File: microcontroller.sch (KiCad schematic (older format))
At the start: 21 parts, among them J4 Conn_01x02, J6 I2C, J7 Conn_01x02, J8 I2C, SW1 SW_Push, U3 ESP32-DEVKIT

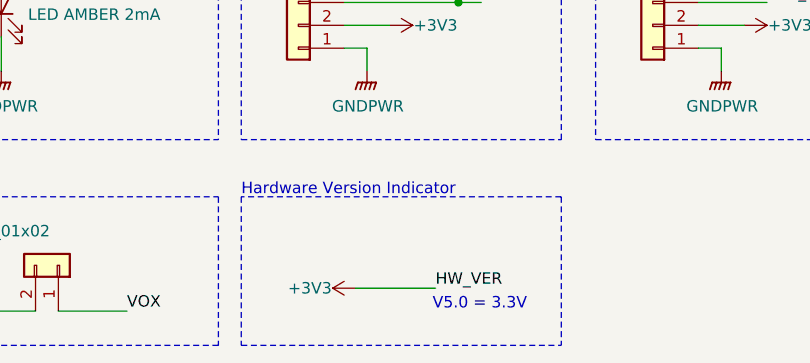
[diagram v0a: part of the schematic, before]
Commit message: Added Pullup to HW indicator [#25]
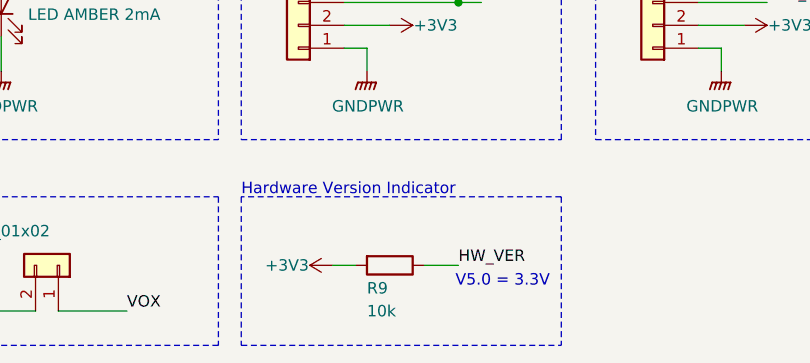
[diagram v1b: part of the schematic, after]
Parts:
- added R9: 10k, Resistor_SMD:R_0805_2012Metric_Pad1.15x1.40mm_HandSolder, symbol Device:R
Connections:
- net +3V3: now also R9.2; no longer U3.5 (IO34)
- new net HW_VER: R9.1, U3.5 (IO34)
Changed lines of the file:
@@
 Text Notes 2250 5700 0    50   ~ 0
 Hardware Version Indicator
-Text Label 3100 6100 0    50   ~ 0
+Text Label 3200 6000 0    50   ~ 0
 HW_VER
 Wire Notes Line
 	2250 6350 3650 6350
-Wire Wire Line
-	2750 6100 3100 6100
-Text Notes 3500 6200 2    50   ~ 0
+Text Notes 3600 6100 2    50   ~ 0
 V5.0 = 3.3V
 Wire Notes Line
 	3650 5700 3650 6350
-Wire Notes Line
-	2250 5700 2250 6350
-Wire Notes Line
-	2150 5700 2150 6350
 Wire Notes Line
 	700  5700 700  6350
@@
 L power:+3V3 #PWR?
 U 1 1 5E2D79C9
-P 2750 6100
+P 2650 6000
 AR Path="/5E2D79C9" Ref="#PWR?"  Part="1"
 AR Path="/5C10B93A/5E2D79C9" Ref="#PWR045"  Part="1"
-F 0 "#PWR045" H 2750 5950 50  0001 C CNN
-F 1 "+3V3" V 2750 6300 50  0000 C CNN
-F 2 "" H 2750 6100 50  0001 C CNN
-F 3 "" H 2750 6100 50  0001 C CNN
-	1    2750 6100
+F 0 "#PWR045" H 2650 5850 50  0001 C CNN
+F 1 "+3V3" V 2650 6200 50  0000 C CNN
+F 2 "" H 2650 6000 50  0001 C CNN
+F 3 "" H 2650 6000 50  0001 C CNN
+	1    2650 6000
 	0    -1   -1   0
 $EndComp
@@
 	1    0    0    -1
 $EndComp
+Wire Notes Line
+	2150 5700 2150 6350
+Wire Notes Line
+	2250 5700 2250 6350
+$Comp
+L Device:R R?
+U 1 1 5E288A63
+P 2900 6000
+AR Path="/5E288A63" Ref="R?"  Part="1"
+AR Path="/5C10B93A/5E288A63" Ref="R9"  Part="1"
+F 0 "R9" V 3000 5900 50  0000 L CNN
+F 1 "10k" V 3100 5900 50  0000 L CNN
+F 2 "Resistor_SMD:R_0805_2012Metric_Pad1.15x1.40mm_HandSolder" V 2830 6000 50  0001 C CNN
+F 3 "~" H 2900 6000 50  0001 C CNN
+F 4 "603-RC0805JR-072K2L " H -5850 2500 50  0001 C CNN "Mouser Best.Nr."
+	1    2900 6000
+	0    1    1    0
+$EndComp
+Wire Wire Line
+	2650 6000 2750 6000
+Wire Wire Line
+	3050 6000 3200 6000
 $EndSCHEMATC

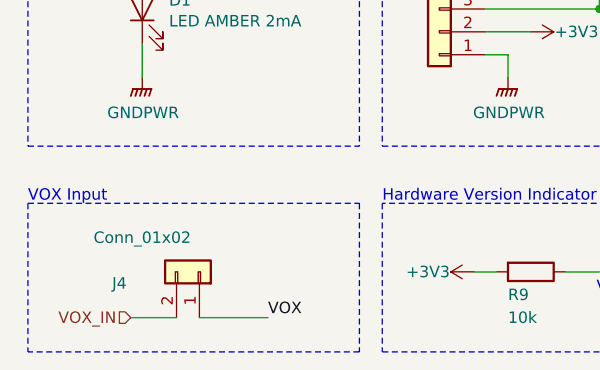
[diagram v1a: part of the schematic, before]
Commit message: PCB enhancements [#25]
* Removed C1 and C2
* Modified symmetric audio path
* Modified VOX path
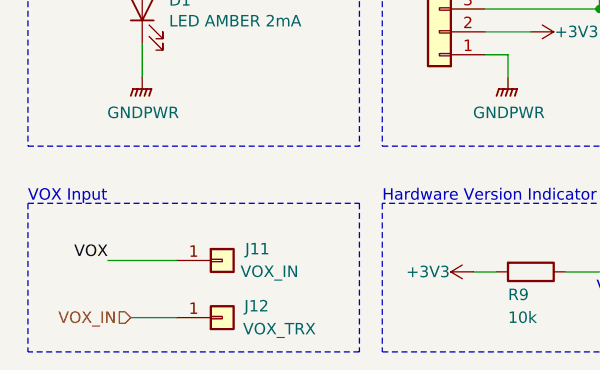
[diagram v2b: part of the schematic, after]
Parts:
- removed J4: Conn_01x02, Connector_PinHeader_2.54mm:PinHeader_1x02_P2.54mm_Vertical, symbol Connector_Generic:Conn_01x02
- added J11: VOX_IN, Connector_PinSocket_2.54mm:PinSocket_1x01_P2.54mm_Vertical, symbol Connector_Generic:Conn_01x01
- added J12: VOX_TRX, Connector_PinSocket_2.54mm:PinSocket_1x01_P2.54mm_Vertical, symbol Connector_Generic:Conn_01x01
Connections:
- net VOX: now also J11.1 (Pin_1)
- net VOX_IN: now also J12.1 (Pin_1)
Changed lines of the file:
@@
 Text HLabel 1150 6200 0    50   Input ~ 0
 VOX_IN
-Text Label 1750 6200 0    50   ~ 0
+Text Label 1050 5950 2    50   ~ 0
 VOX
 Wire Notes Line
@@
 Wire Notes Line
 	700  2000 700  3600
-$Comp
-L Connector_Generic:Conn_01x02 J4
-U 1 1 5E316637
-P 1450 6000
-F 0 "J4" V 1400 5650 50  0000 C CNN
-F 1 "Conn_01x02" V 1600 5750 50  0000 C CNN
-F 2 "Connector_PinHeader_2.54mm:PinHeader_1x02_P2.54mm_Vertical" H 1450 6000 50  0001 C CNN
-F 3 "~" H 1450 6000 50  0001 C CNN
-F 4 " 855-M20-9990246" H 1450 6000 50  0001 C CNN "Mouser Best.Nr."
-	1    1450 6000
-	0    1    -1   0
-$EndComp
-Wire Wire Line
-	1450 6200 1750 6200
+Wire Wire Line
+	1350 5950 1050 5950
 Wire Wire Line
 	1150 6200 1350 6200
@@
 Wire Wire Line
 	3050 6000 3200 6000
+$Comp
+L Connector_Generic:Conn_01x01 J11
+U 1 1 5E2A5603
+P 1550 5950
+F 0 "J11" H 1650 6000 50  0000 L CNN
+F 1 "VOX_IN" H 1630 5901 50  0000 L CNN
+F 2 "Connector_PinSocket_2.54mm:PinSocket_1x01_P2.54mm_Vertical" H 1550 5950 50  0001 C CNN
+F 3 "~" H 1550 5950 50  0001 C CNN
+	1    1550 5950
+	1    0    0    -1
+$EndComp
+$Comp
+L Connector_Generic:Conn_01x01 J12
+U 1 1 5E2BA804
+P 1550 6200
+F 0 "J12" H 1700 6150 50  0000 C CNN
+F 1 "VOX_TRX" H 1800 6250 50  0000 C CNN
+F 2 "Connector_PinSocket_2.54mm:PinSocket_1x01_P2.54mm_Vertical" H 1550 6200 50  0001 C CNN
+F 3 "~" H 1550 6200 50  0001 C CNN
+	1    1550 6200
+	1    0    0    1
+$EndComp
 $EndSCHEMATC

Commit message: BOM Update
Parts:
- J11, J12: DNA (none) -> DNA; Mouser Best.Nr. (none) -> -
- J6, J8: DNA (none) -> DNA
- J7: value Conn_01x02 -> SW1_CON; DNA (none) -> DNA; Mouser Best.Nr. 855-M20-9990246 -> 855-M20-9990246
- R9: Mouser Best.Nr. 603-RC0805JR-072K2L -> 603-RC0805FR-0710KL
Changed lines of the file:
@@
 F 3 "~" H 2500 4950 50  0001 C CNN
 F 4 "855-M20-9770446" H -400 -100 50  0001 C CNN "Mouser Best.Nr."
+F 5 "DNA" H 2500 4950 50  0001 C CNN "DNA"
 	1    2500 4950
 	-1   0    0    1
@@
 P 1650 2950
 F 0 "J7" H 1600 2600 50  0000 C CNN
-F 1 "Conn_01x02" H 1800 2700 50  0000 C CNN
+F 1 "SW1_CON" H 1700 2700 50  0000 C CNN
 F 2 "Connector_PinHeader_2.54mm:PinHeader_1x02_P2.54mm_Vertical" H 1650 2950 50  0001 C CNN
 F 3 "~" H 1650 2950 50  0001 C CNN
-F 4 " 855-M20-9990246" H 1650 2950 50  0001 C CNN "Mouser Best.Nr."
+F 4 "855-M20-9990246" H 1650 2950 50  0001 C CNN "Mouser Best.Nr."
+F 5 "DNA" H 1650 2950 50  0001 C CNN "DNA"
 	1    1650 2950
 	1    0    0    1
@@
 F 3 "~" H 4050 4950 50  0001 C CNN
 F 4 "855-M20-9770446" H 1150 -100 50  0001 C CNN "Mouser Best.Nr."
+F 5 "DNA" H 4050 4950 50  0001 C CNN "DNA"
 	1    4050 4950
 	-1   0    0    1
@@
 F 2 "Resistor_SMD:R_0805_2012Metric_Pad1.15x1.40mm_HandSolder" V 2830 6000 50  0001 C CNN
 F 3 "~" H 2900 6000 50  0001 C CNN
-F 4 "603-RC0805JR-072K2L " H -5850 2500 50  0001 C CNN "Mouser Best.Nr."
+F 4 " 603-RC0805FR-0710KL" H -5850 2500 50  0001 C CNN "Mouser Best.Nr."
 	1    2900 6000
 	0    1    1    0
@@
 F 2 "Connector_PinSocket_2.54mm:PinSocket_1x01_P2.54mm_Vertical" H 1550 5950 50  0001 C CNN
 F 3 "~" H 1550 5950 50  0001 C CNN
+F 4 "DNA" H 1550 5950 50  0001 C CNN "DNA"
+F 5 "-" H 1550 5950 50  0001 C CNN "Mouser Best.Nr."
 	1    1550 5950
 	1    0    0    -1
@@
 F 2 "Connector_PinSocket_2.54mm:PinSocket_1x01_P2.54mm_Vertical" H 1550 6200 50  0001 C CNN
 F 3 "~" H 1550 6200 50  0001 C CNN
+F 4 "DNA" H 1550 6200 50  0001 C CNN "DNA"
+F 5 "-" H 1550 6200 50  0001 C CNN "Mouser Best.Nr."
 	1    1550 6200
 	1    0    0    1

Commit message: Fixed mouser order IDs
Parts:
- R2, R9: Mouser Best.Nr. 603-RC0805FR-0710KL -> 603-RC0805FR-0710KL
- SW1: Mouser Best.Nr. 611-PTS645VK832 -> 611-PTS645VK832
- U3: Mouser Best.Nr. 356-ESP32-DEVKITC32D -> 356-ESP32-DEVKITC32D
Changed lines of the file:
@@
 F 2 "Button_Switch_THT:SW_Tactile_SKHH_Angled" H 950 3300 50  0001 C CNN
 F 3 "" H 950 3300 50  0001 C CNN
-F 4 " 611-PTS645VK832" H -2700 -2500 50  0001 C CNN "Mouser Best.Nr."
+F 4 "611-PTS645VK832" H -2700 -2500 50  0001 C CNN "Mouser Best.Nr."
 	1    950  3100
 	0    -1   -1   0
@@
 F 2 "Resistor_SMD:R_0805_2012Metric_Pad1.15x1.40mm_HandSolder" V 1130 2600 50  0001 C CNN
 F 3 "~" H 1200 2600 50  0001 C CNN
-F 4 " 603-RC0805FR-0710KL" H -3550 -2550 50  0001 C CNN "Mouser Best.Nr."
+F 4 "603-RC0805FR-0710KL" H -3550 -2550 50  0001 C CNN "Mouser Best.Nr."
 	1    1200 2600
 	1    0    0    -1
@@
 F 2 "nodemcu_esp-32s:ESP32-DEVKITC-32D" H 7700 2200 50  0001 L BNN
 F 3 "None" H 7700 2200 50  0001 L BNN
-F 4 " 356-ESP32-DEVKITC32D " H 7700 2200 50  0001 C CNN "Mouser Best.Nr."
+F 4 "356-ESP32-DEVKITC32D " H 7700 2200 50  0001 C CNN "Mouser Best.Nr."
 	1    7700 2200
 	1    0    0    -1
@@
 F 2 "Resistor_SMD:R_0805_2012Metric_Pad1.15x1.40mm_HandSolder" V 2830 6000 50  0001 C CNN
 F 3 "~" H 2900 6000 50  0001 C CNN
-F 4 " 603-RC0805FR-0710KL" H -5850 2500 50  0001 C CNN "Mouser Best.Nr."
+F 4 "603-RC0805FR-0710KL" H -5850 2500 50  0001 C CNN "Mouser Best.Nr."
 	1    2900 6000
 	0    1    1    0

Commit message: Add Digikey Part Numbers
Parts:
- C7: PartNrDigikey (none) -> PCE4214CT-ND
- D1: PartNrDigikey (none) -> 754-1921-1-ND
- D3: PartNrDigikey (none) -> P6SMB16CABBCT-ND
- D4: PartNrDigikey (none) -> 754-1923-1-ND
- D5: PartNrDigikey (none) -> 754-1924-1-ND
- F1: PartNrDigikey (none) -> 507-1799-1-ND
- J6, J8: PartNrDigikey (none) -> 952-1785-ND
- J7: PartNrDigikey (none) -> 952-2262-ND
- L4: PartNrDigikey (none) -> 732-4872-1-ND
- R2, R9: PartNrDigikey (none) -> 311-10.0KCRCT-ND
- R3: PartNrDigikey (none) -> 311-2.2KARCT-ND
- R4, R5: PartNrDigikey (none) -> 311-820ARCT-ND
- R6, R7: PartNrDigikey (none) -> 311-4.7KARCT-ND
- SW1: PartNrDigikey (none) -> CKN10950-ND
- U3: PartNrDigikey (none) -> 1965-1000-ND
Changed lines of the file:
@@
 EESchema Schematic File Version 4
+LIBS:bt-trx-dev-board-cache
 EELAYER 30 0
 EELAYER END
@@
 F 3 "" H 950 3300 50  0001 C CNN
 F 4 "611-PTS645VK832" H -2700 -2500 50  0001 C CNN "Mouser Best.Nr."
+F 5 "CKN10950-ND" H 950 3100 50  0001 C CNN "PartNrDigikey"
 	1    950  3100
 	0    -1   -1   0
@@
 F 3 "~" H 2450 2600 50  0001 C CNN
 F 4 "603-RC0805JR-07820RL" H -2300 -2550 50  0001 C CNN "Mouser Best.Nr."
+F 5 "311-820ARCT-ND" H 2450 2600 50  0001 C CNN "PartNrDigikey"
 	1    2450 2600
 	1    0    0    -1
@@
 F 3 "~" H 2450 3050 50  0001 C CNN
 F 4 "604-APA2107LVBCD" H -2300 -2500 50  0001 C CNN "Mouser Best.Nr."
+F 5 "754-1923-1-ND" H 2450 3050 50  0001 C CNN "PartNrDigikey"
 	1    2450 3050
 	0    -1   -1   0
@@
 F 3 "~" H 2800 2600 50  0001 C CNN
 F 4 "603-RC0805JR-07820RL" H -2300 -2550 50  0001 C CNN "Mouser Best.Nr."
+F 5 "311-820ARCT-ND" H 2800 2600 50  0001 C CNN "PartNrDigikey"
 	1    2800 2600
 	1    0    0    -1
@@
 F 3 "~" H 2800 3050 50  0001 C CNN
 F 4 "604-APA2107LZGCK" H -2300 -2500 50  0001 C CNN "Mouser Best.Nr."
+F 5 "754-1924-1-ND" H 2800 3050 50  0001 C CNN "PartNrDigikey"
 	1    2800 3050
 	0    -1   -1   0
@@
 F 3 "~" H 1400 1050 50  0001 C CNN
 F 4 "530-0ZCJ0025AF2E" H -4000 -50 50  0001 C CNN "Mouser Best.Nr."
+F 5 "507-1799-1-ND" H 1400 1050 50  0001 C CNN "PartNrDigikey"
 	1    1400 1050
 	0    1    1    0
@@
 F 3 "~" H 2300 1050 50  0001 C CNN
 F 4 "710-74438335470" V 2300 1050 50  0001 C CNN "Mouser Best.Nr."
+F 5 "732-4872-1-ND" H 2300 1050 50  0001 C CNN "PartNrDigikey"
 	1    2300 1050
 	0    1    1    0
@@
 F 3 "~" H 2550 1250 50  0001 C CNN
 F 4 "652-P6SMB16CA" V 2550 1250 50  0001 C CNN "Mouser Best.Nr."
+F 5 "P6SMB16CABBCT-ND" H 2550 1250 50  0001 C CNN "PartNrDigikey"
 	1    2550 1250
 	0    1    1    0
@@
 F 3 "~" H 1200 4450 50  0001 C CNN
 F 4 "603-RC0805JR-072K2L " H -7550 950 50  0001 C CNN "Mouser Best.Nr."
+F 5 "311-2.2KARCT-ND" H 1200 4450 50  0001 C CNN "PartNrDigikey"
 	1    1200 4450
 	1    0    0    -1
@@
 F 3 "~" H 1200 4850 50  0001 C CNN
 F 4 "604-APA2107LSECKJ4RV" H -7550 950 50  0001 C CNN "Mouser Best.Nr."
+F 5 "754-1921-1-ND" H 1200 4850 50  0001 C CNN "PartNrDigikey"
 	1    1200 4850
 	0    -1   -1   0
@@
 F 4 "855-M20-9770446" H -400 -100 50  0001 C CNN "Mouser Best.Nr."
 F 5 "DNA" H 2500 4950 50  0001 C CNN "DNA"
+F 6 "952-1785-ND" H 2500 4950 50  0001 C CNN "PartNrDigikey"
 	1    2500 4950
 	-1   0    0    1
@@
 F 3 "~" H 2900 4450 50  0001 C CNN
 F 4 "603-RC0805JR-074K7L" H -750 -700 50  0001 C CNN "Mouser Best.Nr."
+F 5 "311-4.7KARCT-ND" H 2900 4450 50  0001 C CNN "PartNrDigikey"
 	1    2900 4450
 	1    0    0    -1
@@
 F 3 "~" H 3200 4450 50  0001 C CNN
 F 4 "603-RC0805JR-074K7L" H -450 -700 50  0001 C CNN "Mouser Best.Nr."
+F 5 "311-4.7KARCT-ND" H 3200 4450 50  0001 C CNN "PartNrDigikey"
 	1    3200 4450
 	1    0    0    -1
@@
 F 3 "~" H 3050 1250 50  0001 C CNN
 F 4 "667-EEE-HA1H221P " H 500 0   50  0001 C CNN "Mouser Best.Nr."
+F 5 "PCE4214CT-ND" H 3050 1250 50  0001 C CNN "PartNrDigikey"
 	1    3050 1250
 	1    0    0    -1
@@
 F 4 "855-M20-9990246" H 1650 2950 50  0001 C CNN "Mouser Best.Nr."
 F 5 "DNA" H 1650 2950 50  0001 C CNN "DNA"
+F 6 "952-2262-ND" H 1650 2950 50  0001 C CNN "PartNrDigikey"
 	1    1650 2950
 	1    0    0    1
@@
 F 3 "~" H 1200 2600 50  0001 C CNN
 F 4 "603-RC0805FR-0710KL" H -3550 -2550 50  0001 C CNN "Mouser Best.Nr."
+F 5 "311-10.0KCRCT-ND" H 1200 2600 50  0001 C CNN "PartNrDigikey"
 	1    1200 2600
 	1    0    0    -1
@@
 F 4 "855-M20-9770446" H 1150 -100 50  0001 C CNN "Mouser Best.Nr."
 F 5 "DNA" H 4050 4950 50  0001 C CNN "DNA"
+F 6 "952-1785-ND" H 4050 4950 50  0001 C CNN "PartNrDigikey"
 	1    4050 4950
 	-1   0    0    1
@@
 F 3 "None" H 7700 2200 50  0001 L BNN
 F 4 "356-ESP32-DEVKITC32D " H 7700 2200 50  0001 C CNN "Mouser Best.Nr."
+F 5 "1965-1000-ND" H 7700 2200 50  0001 C CNN "PartNrDigikey"
 	1    7700 2200
 	1    0    0    -1
@@
 F 3 "~" H 2900 6000 50  0001 C CNN
 F 4 "603-RC0805FR-0710KL" H -5850 2500 50  0001 C CNN "Mouser Best.Nr."
+F 5 "311-10.0KCRCT-ND" H 2900 6000 50  0001 C CNN "PartNrDigikey"
 	1    2900 6000
 	0    1    1    0
